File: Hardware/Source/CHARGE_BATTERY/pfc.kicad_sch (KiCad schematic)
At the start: 2 parts, among them U1 UCC28180D

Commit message: hardware:sche:update PFC
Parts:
- added C1, C2: 100nF, 275VAC, charge_battery_footprint_lib:CAP_B32671P-10--5x11x13_TDK, symbol charge_battery_sym_lib:Film Cap
- added F1: 250VAC/7A, charge_battery_footprint_lib:FUSAD2722W65L2250D600, symbol charge_battery_sym_lib:FUSE_250VAC_7A
- added J1: HB9500M-9.5-3P, charge_battery_footprint_lib:CONN3_HB9500_KAN, symbol charge_battery_sym_lib:HB9500M-9.5-3P
- added L1: SS11VL-R05350, charge_battery_footprint_lib:IND_SS11VL-R05350_KEM, symbol charge_battery_sym_lib:SS11VL-R05350
- added RV1: 470V, charge_battery_footprint_lib:MOV07D471K, symbol charge_battery_sym_lib:MOV-07D471K
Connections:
- new net: C1.1, J1.2, L1.1, RV1.1
- new net: C1.2, F1.2, L1.4, RV1.2
- new net: C2.1, L1.2
- new net: C2.2, L1.3
- new net: F1.1, J1.1
- new net Earth: J1.3
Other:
- note added: "Earth"
- note added: "Line"
- note added: "Neutral"
- moved on the sheet: CR1, U1

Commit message: update lib hardware
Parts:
- added D1: KBPC606, charge_battery_footprint_lib:TO_BPC606_VIS, symbol charge_battery_sym_lib:KBPC606
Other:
- moved on the sheet: C1, C2, CR1, L1, RV1

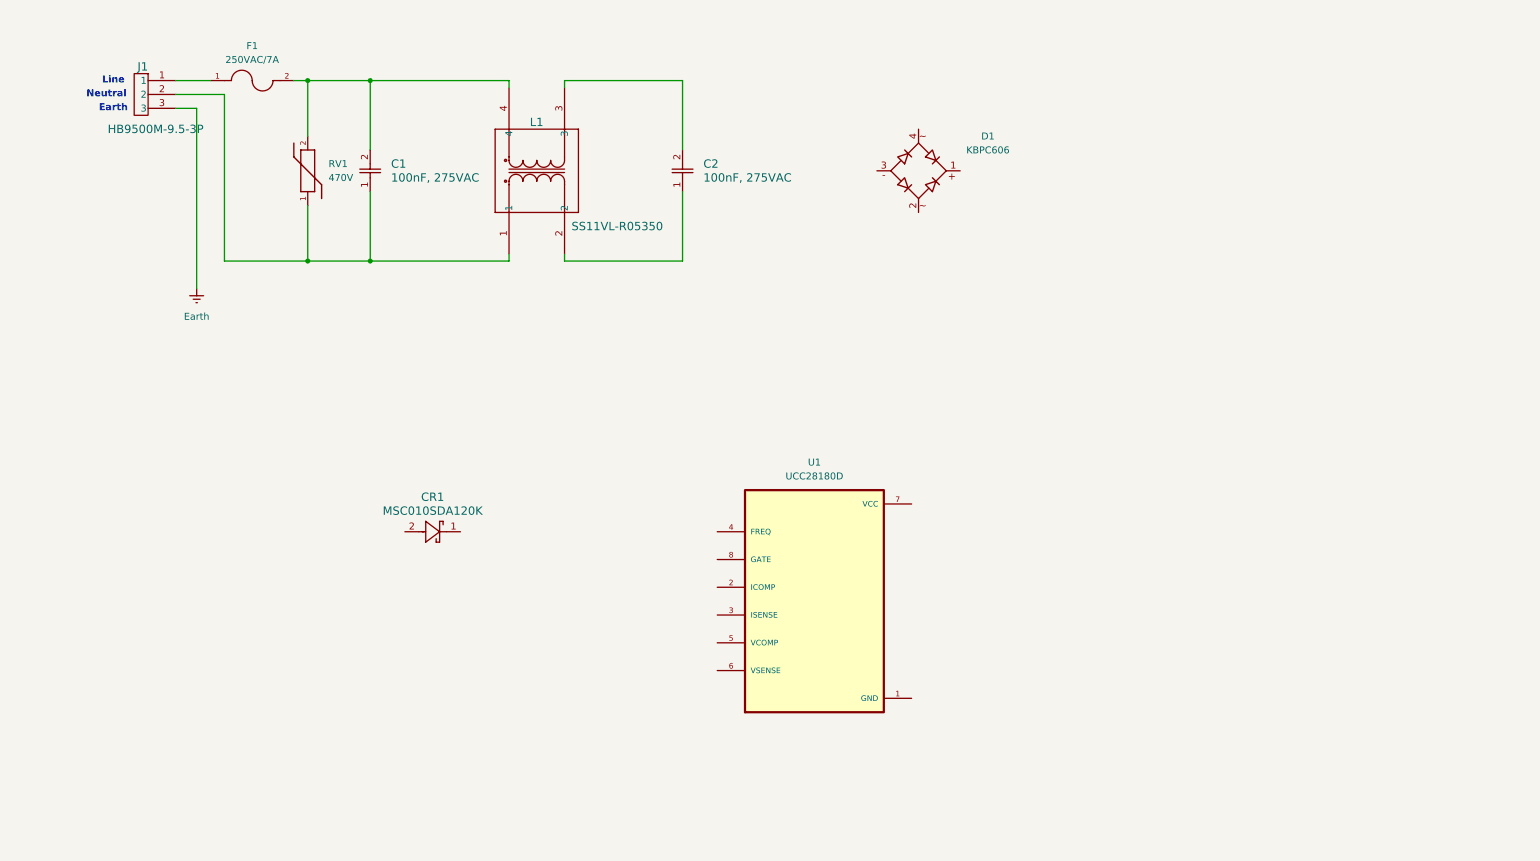
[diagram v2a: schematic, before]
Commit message: update PFC schematic and library
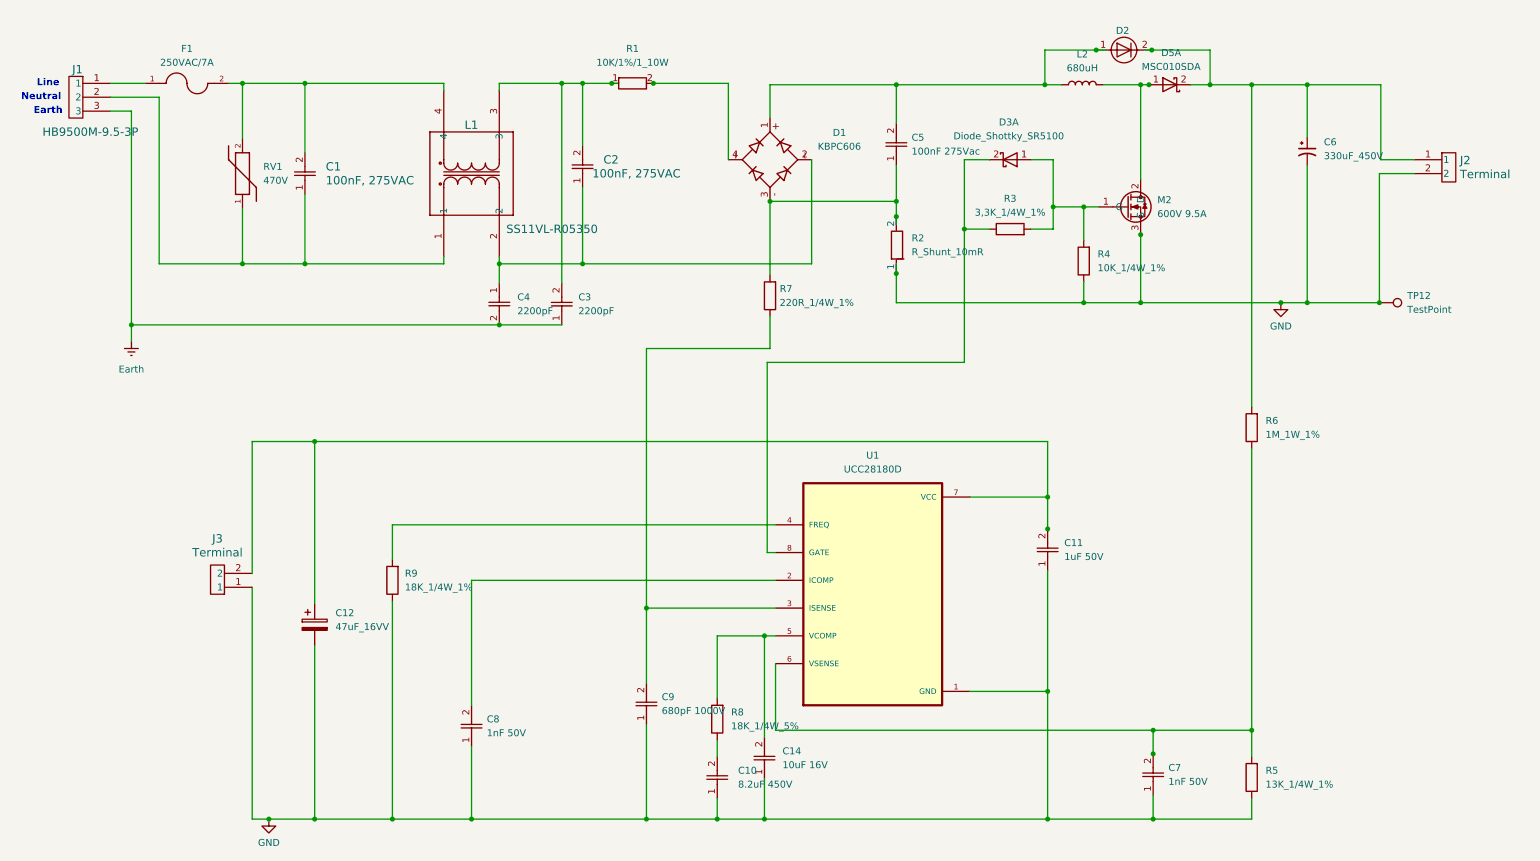
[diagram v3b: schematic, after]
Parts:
- removed CR1: MSC010SDA120K, charge_battery_footprint_lib:TO-220-2_MCH, symbol charge_battery_sym_lib:MSC010SDA120K
- added C10: 8.2uF 450V, charge_battery_footprint_lib:Ceramic_Cap_Hole_8.2uF_450V, symbol charge_battery_sym_lib:Ceramic_Cap_Hole_8.2uF_450V
- added C11: 1uF 50V, charge_battery_footprint_lib:Ceramic_Cap_Hole_1uF_50V, symbol charge_battery_sym_lib:Ceramic_Cap_Hole_1uF_50V_
- added C12: 47uF_16VV, charge_battery_footprint_lib:Cap_Polarized_SMD_47uF_16V, symbol charge_battery_sym_lib:Cap_Polarized_SMD_47uF_16V
- added C14: 10uF 16V, charge_battery_footprint_lib:Ceramic_Cap_10uF_16V, symbol charge_battery_sym_lib:Ceramic_Cap_SMD_10uF_16V
- added C3, C4: 2200pF, charge_battery_footprint_lib:Ceramic_Cap_10uF_16V, symbol charge_battery_sym_lib:Ceramic_Cap_SMD_10uF_16V
- added C5: 100nF 275Vac, charge_battery_footprint_lib:Ceramic_Cap_10uF_16V, symbol charge_battery_sym_lib:Candy_Cap_hole_100nF_275V
- added C6: 330uF_450V, charge_battery_footprint_lib:Big_Cap_330uF_450V, symbol charge_battery_sym_lib:Cap_Polarized_330uF_450V
- added C7, C8: 1nF 50V, charge_battery_footprint_lib:Ceramic_Cap_Hole_1nF_50V, symbol charge_battery_sym_lib:Ceramic_Cap_Hole_1nF_50V
- added C9: 680pF 1000V, charge_battery_footprint_lib:Ceramic_Cap_Hole_680pF_1000V, symbol charge_battery_sym_lib:Ceramic_Cap_Hole_1nF_2000V
- added D2: 60A, 600V, charge_battery_footprint_lib:Diode_FRED_TO247, symbol charge_battery_sym_lib:Diode_DSEI60-06A_FRED_TO247
- added D3: Diode_Shottky_SR5100, charge_battery_footprint_lib:Diode_Schottky_SR5100, symbol charge_battery_sym_lib:Diode_Shottky_SR5100
- added D5: MSC010SDA, charge_battery_footprint_lib:DBoost, symbol charge_battery_sym_lib:Diode_Shottky_DBoost
- added J2, J3: Terminal, charge_battery_footprint_lib:Terminal, symbol charge_battery_sym_lib:Terminal HB9500-2
- added L2: 680uH, Inductor_SMD:L_12x12mm_H8mm, symbol Device:L
- added M2: 600V 9.5A, charge_battery_footprint_lib:MOSFET_FQPF10N60C, symbol charge_battery_sym_lib:MOSFET_FQPF10N60C
- added R1: 10K/1%/1_10W, charge_battery_footprint_lib:Res_10K_0603, symbol charge_battery_sym_lib:Res_10K_0603_1%
- added R2: R_Shunt_10mR, charge_battery_footprint_lib:R_Shunt, symbol charge_battery_sym_lib:R_Shunt_10mR
- added R3: 3,3K_1/4W_1%, charge_battery_footprint_lib:Res_3.3R_1_4W_1, symbol charge_battery_sym_lib:Res_hole_3,3K_1/4W_1%
- added R4: 10K_1/4W_1%, charge_battery_footprint_lib:Res_10K_1_4W_1%, symbol charge_battery_sym_lib:Res_hole_10K_1/4W_1%
- added R5: 13K_1/4W_1%, charge_battery_footprint_lib:Res_13K_1_4W_1, symbol charge_battery_sym_lib:Res_hole_13K_1/4W_1%
- added R6: 1M_1W_1%, charge_battery_footprint_lib:Res_1M_1W_1%, symbol charge_battery_sym_lib:Res_hole_1M_1W_1%
- added R7: 220R_1/4W_1%, charge_battery_footprint_lib:Res_220R_1_4W_1%, symbol charge_battery_sym_lib:Res_hole_220R_1/4W_1%
- added R8: 18K_1/4W_5%, charge_battery_footprint_lib:Res_220R_1_4W_1%, symbol charge_battery_sym_lib:Res_hole_18K_1/4W_1%
- added R9: 18K_1/4W_1%, charge_battery_footprint_lib:Res_220R_1_4W_1%, symbol charge_battery_sym_lib:Res_hole_18K_1/4W_1%
- added TP12: TestPoint, symbol Connector:TestPoint
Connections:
- net Earth: now also C3.1, C4.2
- net at C2.1, L1.2: now also D1.2, C4.1
- net at C2.2, L1.3: now also C3.2, R1.1
- net GND: now reaches U1.1 (GND)
- net GND: now also C10.1, C11.1, C12.2, C14.1, C6.2, C7.1, C8.1, C9.1, J2.2, J3.1, M2.3 (S), R2.1, R4.1, R5.1, R9.1, TP12.1
- net at U1.2 (ICOMP): now also C8.2
- net at U1.3 (ISENSE): now also C9.2, R7.1
- net at U1.4 (FREQ): now also R9.2
- net at U1.5 (VCOMP): now also C14.2, R8.2
- net at U1.6 (VSENSE): now also C7.2, R5.2, R6.1
- net at U1.7 (VCC): now also C11.2, C12.1, J3.2
- net at U1.8 (GATE): now also D3.2 (A), R3.1
- net at D1.1: now also C5.2, D2.1, L2.1
- net at D1.3: now also C5.1, R2.2, R7.2
- net at D1.4: now also R1.2
- new net: D3.1 (K), M2.1 (G), R3.2, R4.2
- new net: C6.1, D2.2, D5.2 (A), J2.1, R6.2
- new net: C10.2, R8.1
- new net: D5.1 (K), L2.2, M2.2 (D)
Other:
- moved on the sheet: C1, C2, D1, F1, J1, L1, RV1, U1

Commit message: update
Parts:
- removed C10: 8.2uF 450V, charge_battery_footprint_lib:Ceramic_Cap_Hole_8.2uF_450V, symbol charge_battery_sym_lib:Ceramic_Cap_Hole_8.2uF_450V
- removed C3, C4: 2200pF, charge_battery_footprint_lib:Ceramic_Cap_10uF_16V, symbol charge_battery_sym_lib:Ceramic_Cap_SMD_10uF_16V
- removed C5: 100nF 275Vac, charge_battery_footprint_lib:Ceramic_Cap_10uF_16V, symbol charge_battery_sym_lib:Candy_Cap_hole_100nF_275V
- removed R1: 10K/1%/1_10W, charge_battery_footprint_lib:Res_10K_0603, symbol charge_battery_sym_lib:Res_10K_0603_1%
- removed TP12: TestPoint, symbol Connector:TestPoint
- added C10: 10uF_50V, Capacitor_SMD:C_0805_2012Metric, symbol charge_battery_sym_lib:Ceramic_Cap_Hole_10uF_50V
- added C3, C4: 1nF 2000V, charge_battery_footprint_lib:Ceramic_Cap_Hole_1nF_2000V, symbol charge_battery_sym_lib:Ceramic_Cap_Hole_680pF_1000V
- added C5: 100nF, 275VAC, charge_battery_footprint_lib:CAP_B32671P-10--5x11x13_TDK, symbol charge_battery_sym_lib:Film Cap
- added TH1: 5R, charge_battery_footprint_lib:Thermistor_NTC, symbol charge_battery_sym_lib:Thermistor_NTC
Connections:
- net Earth: now also C3.1, C4.1
- net GND: now also C10.1
- net at D1.3, R2.2, R7.2: now also C5.1
- net at D1.1, D2.1, L2.1: now also C5.2
- net at C2.2, L1.3: now also C4.2, TH1.1
- net at D1.4: now also TH1.2
- net at C2.1, D1.2, L1.2: now also C3.2
- net at R8.1: now also C10.2
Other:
- moved on the sheet: C11

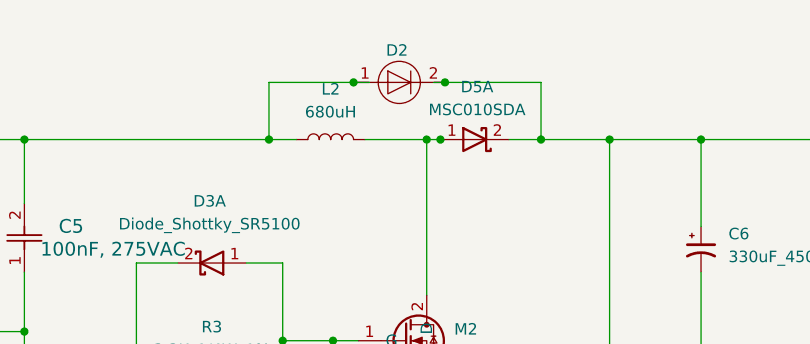
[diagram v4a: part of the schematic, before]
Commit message: update library: res symbol, change grid to 50mil
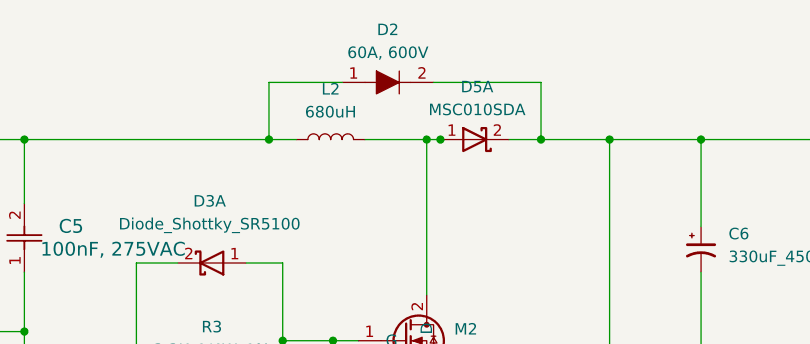
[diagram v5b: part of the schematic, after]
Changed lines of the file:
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@@
 	)
 	(junction
-		(at 211.582 18.542)
-		(diameter 0)
-		(color 0 0 0 0)
-	)
-	(junction
 		(at 117.602 57.658)
 		(diameter 0)
@@
 	)
 	(junction
-		(at 221.742 18.542)
-		(diameter 0)
-		(color 0 0 0 0)
-	)
-	(junction
 		(at 175.006 24.892)
 		(diameter 0)
@@
 	(wire
 		(pts
-			(xy 202.184 18.542) (xy 211.582 18.542)
+			(xy 202.184 18.542) (xy 210.312 18.542)
 		)
 		(stroke
@@
 	(wire
 		(pts
-			(xy 211.582 18.542) (xy 213.36 18.542)
-		)
-		(stroke
-			(width 0)
-			(type default)
-		)
-	)
-	(wire
-		(pts
 			(xy 82.804 105.41) (xy 152.908 105.41)
 		)
@@
 	(wire
 		(pts
+			(xy 220.472 18.542) (xy 232.41 18.542)
+		)
+		(stroke
+			(width 0)
+			(type default)
+		)
+	)
+	(wire
+		(pts
 			(xy 232.41 24.892) (xy 240.03 24.892)
 		)
@@
 		)
 	)
-	(wire
-		(pts
-			(xy 220.472 18.542) (xy 221.742 18.542)
-		)
-		(stroke
-			(width 0)
-			(type default)
-		)
-	)
-	(wire
-		(pts
-			(xy 221.742 18.542) (xy 232.41 18.542)
-		)
-		(stroke
-			(width 0)
-			(type default)
-		)
-	)
 	(text "Neutral"
 		(exclude_from_sim no)
@@
 	)
 	(symbol
-		(lib_id "charge_battery_sym_lib:Diode_DSEI60-06A_FRED_TO247")
-		(at 216.662 18.542 0)
-		(unit 1)
-		(exclude_from_sim no)
-		(in_bom yes)
-		(on_board yes)
-		(dnp no)
-		(property "Reference" "D2"
-			(at 216.408 14.986 0)
-			(effects
-				(font
-					(size 1.27 1.27)
-				)
-			)
-		)
-		(property "Value" "60A, 600V"
-			(at 217.17 15.24 0)
-			(effects
-				(font
-					(size 1.27 1.27)
-				)
-				(hide yes)
-			)
-		)
-		(property "Footprint" "charge_battery_footprint_lib:Diode_FRED_TO247"
-			(at 208.026 12.446 0)
-			(effects
-				(font
-					(size 1.27 1.27)
-					(italic yes)
-				)
-				(hide yes)
-			)
-		)
-		(property "Datasheet" "https://www.lcsc.com/datasheet/lcsc_datasheet_1912111437_Littelfuse-IXYS-DSEI60-06A_C426674.pdf"
-			(at 208.026 12.446 0)
-			(effects
-				(font
-					(size 1.27 1.27)
-					(italic yes)
-				)
-				(hide yes)
-			)
-		)
-		(property "Description" "60A, 600V, Diode Fred, TO-247AD"
-			(at 208.026 12.446 0)
-			(effects
-				(font
-					(size 1.27 1.27)
-				)
-				(hide yes)
-			)
-		)
-		(property "Supply URL" "https://www.thegioiic.com/dsei60-06a-diode-chinh-luu-60a-600v"
-			(at 216.662 8.89 0)
-			(effects
-				(font
-					(size 1.27 1.27)
-				)
-				(hide yes)
-			)
-		)
-		(property "Supply part name" "DSEI60-06A Diode Chỉnh Lưu 60A 600V"
-			(at 216.662 11.43 0)
-			(effects
-				(font
-					(size 1.27 1.27)
-				)
-				(hide yes)
-			)
-		)
-		(property "Supply name" "Thegioiic"
-			(at 216.662 13.97 0)
-			(effects
-				(font
-					(size 1.27 1.27)
-				)
-				(hide yes)
-			)
-		)
-		(pin "1"
-		)
-		(pin "2"
-		)
-		(instances
-			(project "CHARGE_BATTERY"
-				(path "/52eaef32-c16d-4834-ac94-ac67b58aa1d2/8ed7224f-e87e-4b5a-90e5-5ed551abe146"
-					(reference "D2")
-					(unit 1)
-				)
-			)
-		)
-	)
-	(symbol
 		(lib_id "charge_battery_sym_lib:Cap_Polarized_SMD_47uF_16V")
 		(at 68.58 123.698 0)
@@
 					(unit 1)
 				)
+			)
+		)
+	)
+	(symbol
+		(lib_id "charge_battery_sym_lib:Diode_DSEI60-06A_FRED_TO247")
+		(at 215.392 18.542 0)
+		(unit 1)
+		(exclude_from_sim no)
+		(in_bom yes)
+		(on_board yes)
+		(dnp no)
+		(fields_autoplaced yes)
+		(property "Reference" "D2"
+			(at 215.392 12.7 0)
+			(effects
+				(font
+					(size 1.27 1.27)
+				)
+			)
+		)
+		(property "Value" "60A, 600V"
+			(at 215.392 15.24 0)
+			(effects
+				(font
+					(size 1.27 1.27)
+				)
+			)
+		)
+		(property "Footprint" "charge_battery_footprint_lib:Diode_FRED_TO247"
+			(at 206.756 12.446 0)
+			(effects
+				(font
+					(size 1.27 1.27)
+					(italic yes)
+				)
+				(hide yes)
+			)
+		)
+		(property "Datasheet" "https://www.lcsc.com/datasheet/lcsc_datasheet_1912111437_Littelfuse-IXYS-DSEI60-06A_C426674.pdf"
+			(at 206.756 12.446 0)
+			(effects
+				(font
+					(size 1.27 1.27)
+					(italic yes)
+				)
+				(hide yes)
+			)
+		)
+		(property "Description" "60A, 600V, Diode Fred, TO-247AD"
+			(at 206.756 12.446 0)
+			(effects
+				(font
+					(size 1.27 1.27)
+				)
+				(hide yes)
+			)
+		)
+		(property "Supply URL" "https://www.thegioiic.com/dsei60-06a-diode-chinh-luu-60a-600v"
+			(at 198.882 12.192 0)
+			(effects
+				(font
+					(size 1.27 1.27)
+				)
+				(hide yes)
+			)
+		)
+		(property "Supply part name" "DSEI60-06A Diode Chỉnh Lưu 60A 600V"
+			(at 193.294 12.192 0)
+			(effects
+				(font
+					(size 1.27 1.27)
+				)
+				(hide yes)
+			)
+		)
+		(property "Supply name" "Thegioiic"
+			(at 195.326 12.446 0)
+			(effects
+				(font
+					(size 1.27 1.27)
+				)
+				(hide yes)
+			)
+		)
+		(pin "1"
+		)
+		(pin "2"
+		)
+		(instances
+			(project "CHARGE_BATTERY"
+				(path "/52eaef32-c16d-4834-ac94-ac67b58aa1d2/8ed7224f-e87e-4b5a-90e5-5ed551abe146"
+					(reference "D2")
+					(unit 1)
+				)
